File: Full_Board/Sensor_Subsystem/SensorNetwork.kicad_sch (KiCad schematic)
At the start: 34 parts, among them J12 OQ0432500000G, J13 OQ0432500000G, J14 OQ0432500000G, J15 OQ0432500000G, J16 OQ0432500000G, J17 OQ0432500000G, J18 OQ0432500000G, J19 OQ0432500000G, U13 UCLAMP3301H.TCT, U14 UCLAMP3301H.TCT, U15 SN74LV4051ATPWRQ1, U16 SN74LV4051ATPWRQ1

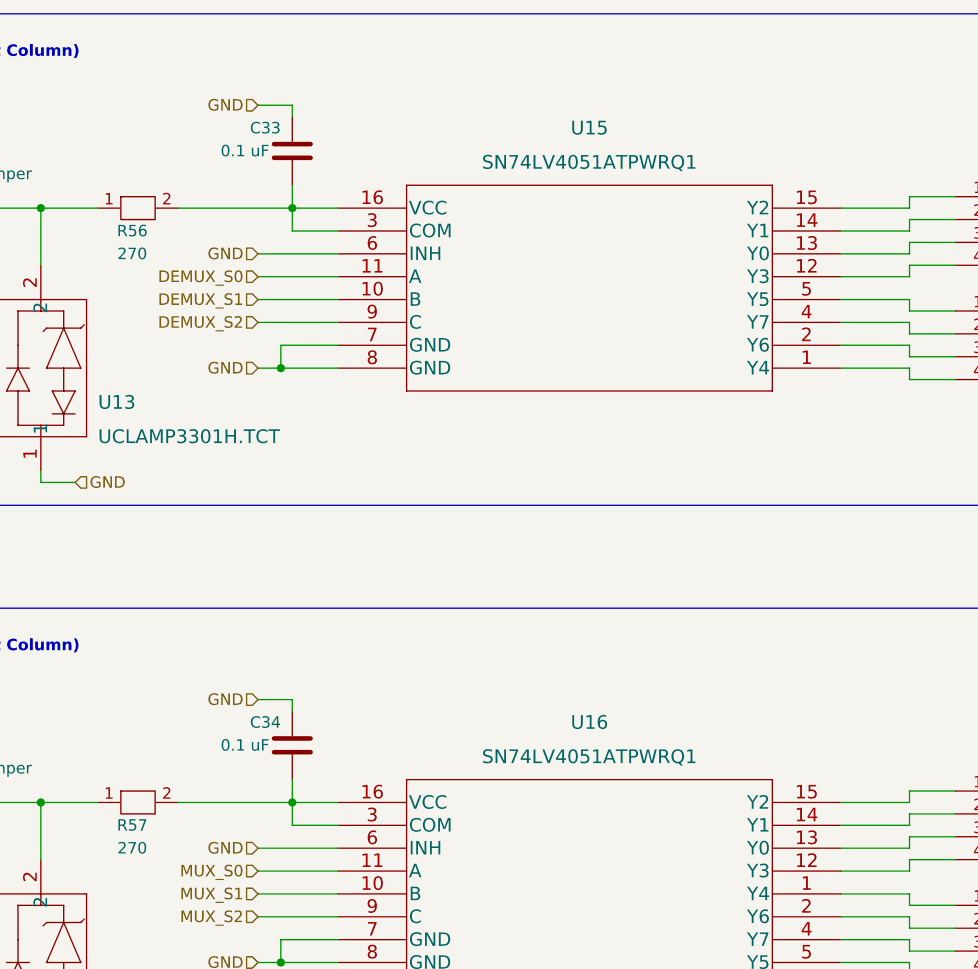
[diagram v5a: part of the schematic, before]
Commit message: Replaced electromagnet IC and fixed ERC errors with stepper driver
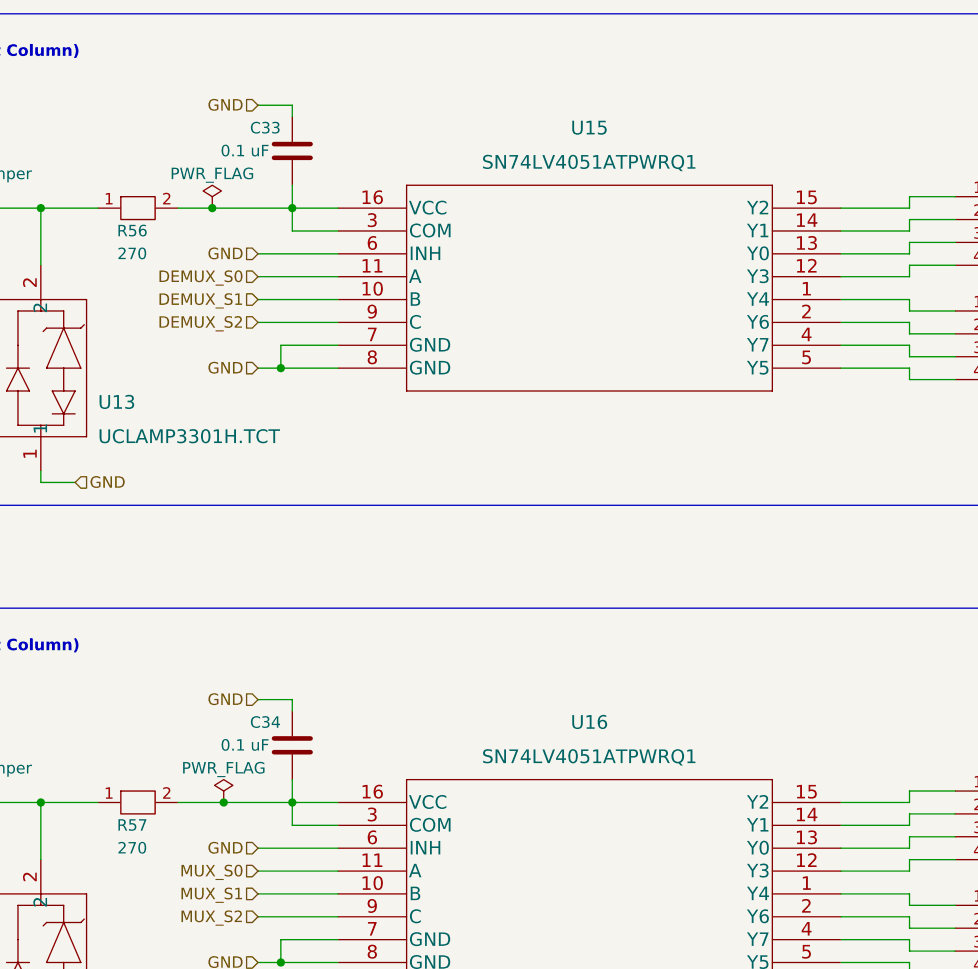
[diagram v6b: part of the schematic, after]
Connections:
- net at U15.1 (Y4): now also J13.1; no longer J13.4
- net at U15.2 (Y6): now also J13.2; no longer J13.3
- net at U15.4 (Y7): now also J13.3; no longer J13.2
- net at U15.5 (Y5): now also J13.4; no longer J13.1
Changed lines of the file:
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@@
   (junction (at 245.11 149.86) (diameter 0) (color 0 0 0 0)
   )
+  (junction (at 69.85 128.27) (diameter 0) (color 0 0 0 0)
+  )
   (junction (at 77.47 62.23) (diameter 0) (color 0 0 0 0)
   )
+  (junction (at 68.58 62.23) (diameter 0) (color 0 0 0 0)
+  )
   (wire (pts (xy 207.01 138.43) (xy 207.01 135.89))
     (stroke (width 0) (type default) (color 0 0 0 0))
@@
     (stroke (width 0) (type default) (color 0 0 0 0))
   )
-  (wire (pts (xy 64.77 128.27) (xy 77.47 128.27))
+  (wire (pts (xy 64.77 128.27) (xy 69.85 128.27))
     (stroke (width 0) (type default) (color 0 0 0 0))
   )
@@
     (stroke (width 0) (type default) (color 0 0 0 0))
   )
+  (wire (pts (xy 69.85 128.27) (xy 77.47 128.27))
+    (stroke (width 0) (type default) (color 0 0 0 0))
+  )
   (wire (pts (xy 265.43 72.39) (xy 265.43 73.66))
     (stroke (width 0) (type default) (color 0 0 0 0))
@@
     (stroke (width 0) (type default) (color 0 0 0 0))
   )
+  (wire (pts (xy 68.58 62.23) (xy 77.47 62.23))
+    (stroke (width 0) (type default) (color 0 0 0 0))
+  )
   (wire (pts (xy 77.47 59.69) (xy 77.47 62.23))
     (stroke (width 0) (type default) (color 0 0 0 0))
@@
     (stroke (width 0) (type default) (color 0 0 0 0))
   )
-  (wire (pts (xy 64.77 62.23) (xy 77.47 62.23))
+  (wire (pts (xy 64.77 62.23) (xy 68.58 62.23))
     (stroke (width 0) (type default) (color 0 0 0 0))
   )
@@
     (pin "1")
     (pin "2")
+  )
+  (symbol (lib_id "power:PWR_FLAG") (at 68.58 62.23 0) (unit 1)
+    (in_bom yes) (on_board yes)
+    (property "Reference" "#FLG0101" (id 0) (at 68.58 60.325 0)
+      (effects (font (size 1.27 1.27)) hide)
+    )
+    (property "Value" "PWR_FLAG" (id 1) (at 68.58 58.42 0))
+    (property "Footprint" "" (id 2) (at 68.58 62.23 0)
+      (effects (font (size 1.27 1.27)) hide)
+    )
+    (property "Datasheet" "~" (id 3) (at 68.58 62.23 0)
+      (effects (font (size 1.27 1.27)) hide)
+    )
+    (pin "1")
   )
   (symbol (lib_id "Device:C") (at 77.47 121.92 0) (mirror y) (unit 1)
@@
     (pin "2")
   )
-  (symbol (lib_name "SN74LV4051ATPWRQ1_1") (lib_id "SN74LV4051ATPWRQ1:SN74LV4051ATPWRQ1") (at 82.55 64.77 0) (unit 1)
+  (symbol (lib_id "SN74LV4051ATPWRQ1:SN74LV4051ATPWRQ1") (at 82.55 64.77 0) (unit 1)
     (in_bom yes) (on_board yes) (fields_autoplaced)
     (property "Reference" "U15" (id 0) (at 110.49 53.34 0)
@@
     (pin "9")
   )
+  (symbol (lib_id "power:PWR_FLAG") (at 69.85 128.27 0) (unit 1)
+    (in_bom yes) (on_board yes)
+    (property "Reference" "#FLG0102" (id 0) (at 69.85 126.365 0)
+      (effects (font (size 1.27 1.27)) hide)
+    )
+    (property "Value" "PWR_FLAG" (id 1) (at 69.85 124.46 0))
+    (property "Footprint" "" (id 2) (at 69.85 128.27 0)
+      (effects (font (size 1.27 1.27)) hide)
+    )
+    (property "Datasheet" "~" (id 3) (at 69.85 128.27 0)
+      (effects (font (size 1.27 1.27)) hide)
+    )
+    (pin "1")
+  )
   (symbol (lib_id "OQ04325500000G:OQ0432500000G") (at 248.92 135.89 90) (unit 1)

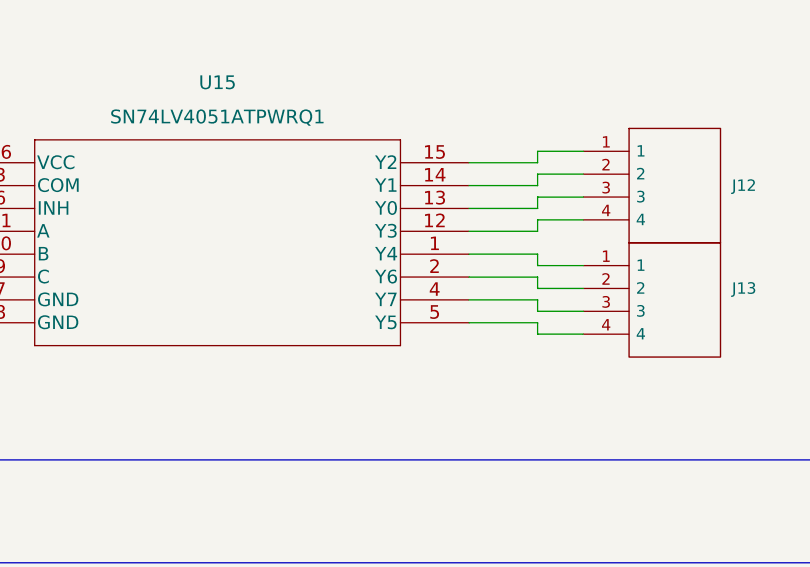
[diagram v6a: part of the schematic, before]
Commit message: Added traces for emag and increased the width of some power lines
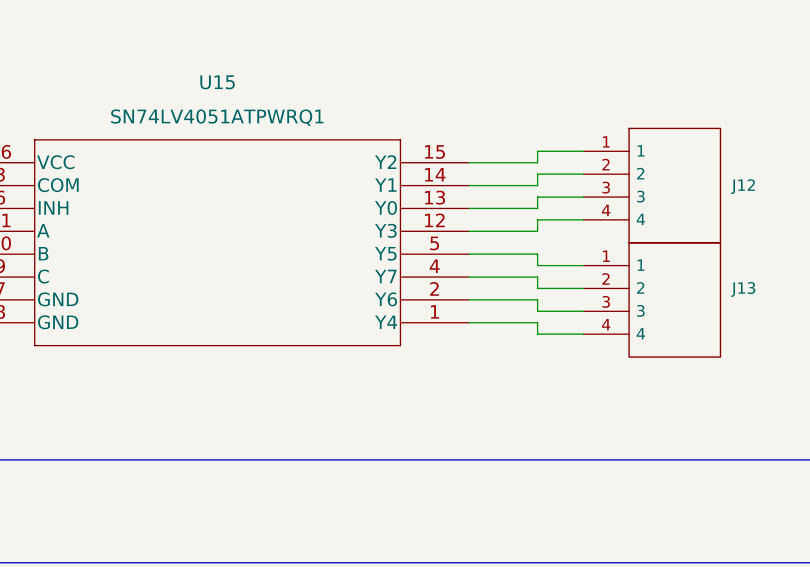
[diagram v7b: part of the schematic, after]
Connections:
- net at U15.1 (Y4): now also J13.4; no longer J13.1
- net at U15.2 (Y6): now also J13.3; no longer J13.2
- net at U15.4 (Y7): now also J13.2; no longer J13.3
- net at U15.5 (Y5): now also J13.1; no longer J13.4
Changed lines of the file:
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@@
     (pin "2")
   )
-  (symbol (lib_id "SN74LV4051ATPWRQ1:SN74LV4051ATPWRQ1") (at 82.55 64.77 0) (unit 1)
+  (symbol (lib_name "SN74LV4051ATPWRQ1_1") (lib_id "SN74LV4051ATPWRQ1:SN74LV4051ATPWRQ1") (at 82.55 64.77 0) (unit 1)
     (in_bom yes) (on_board yes) (fields_autoplaced)
     (property "Reference" "U15" (id 0) (at 110.49 53.34 0)

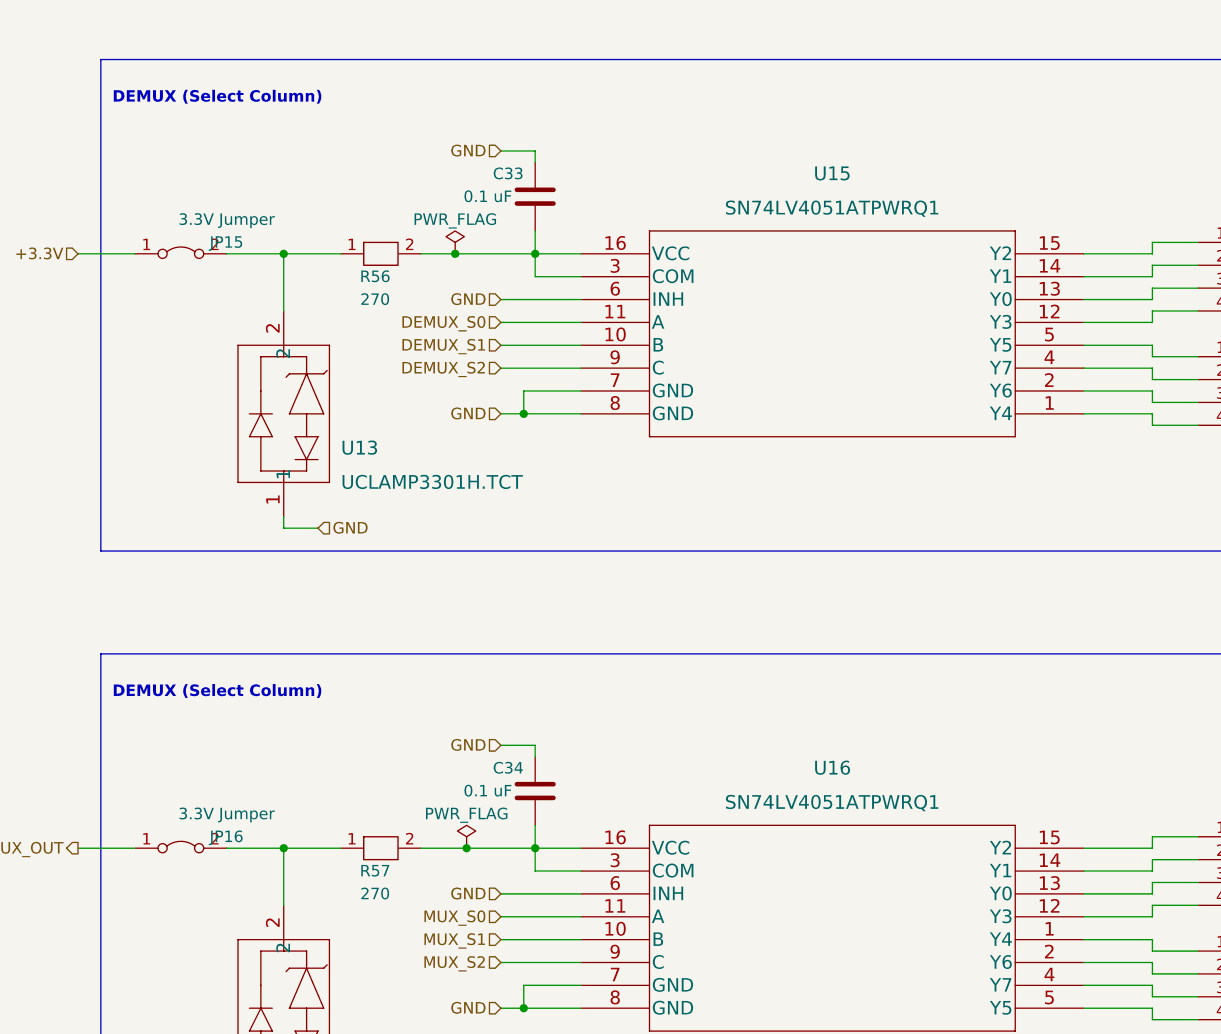
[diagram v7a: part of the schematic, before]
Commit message: Cleanup all schematics and project libs
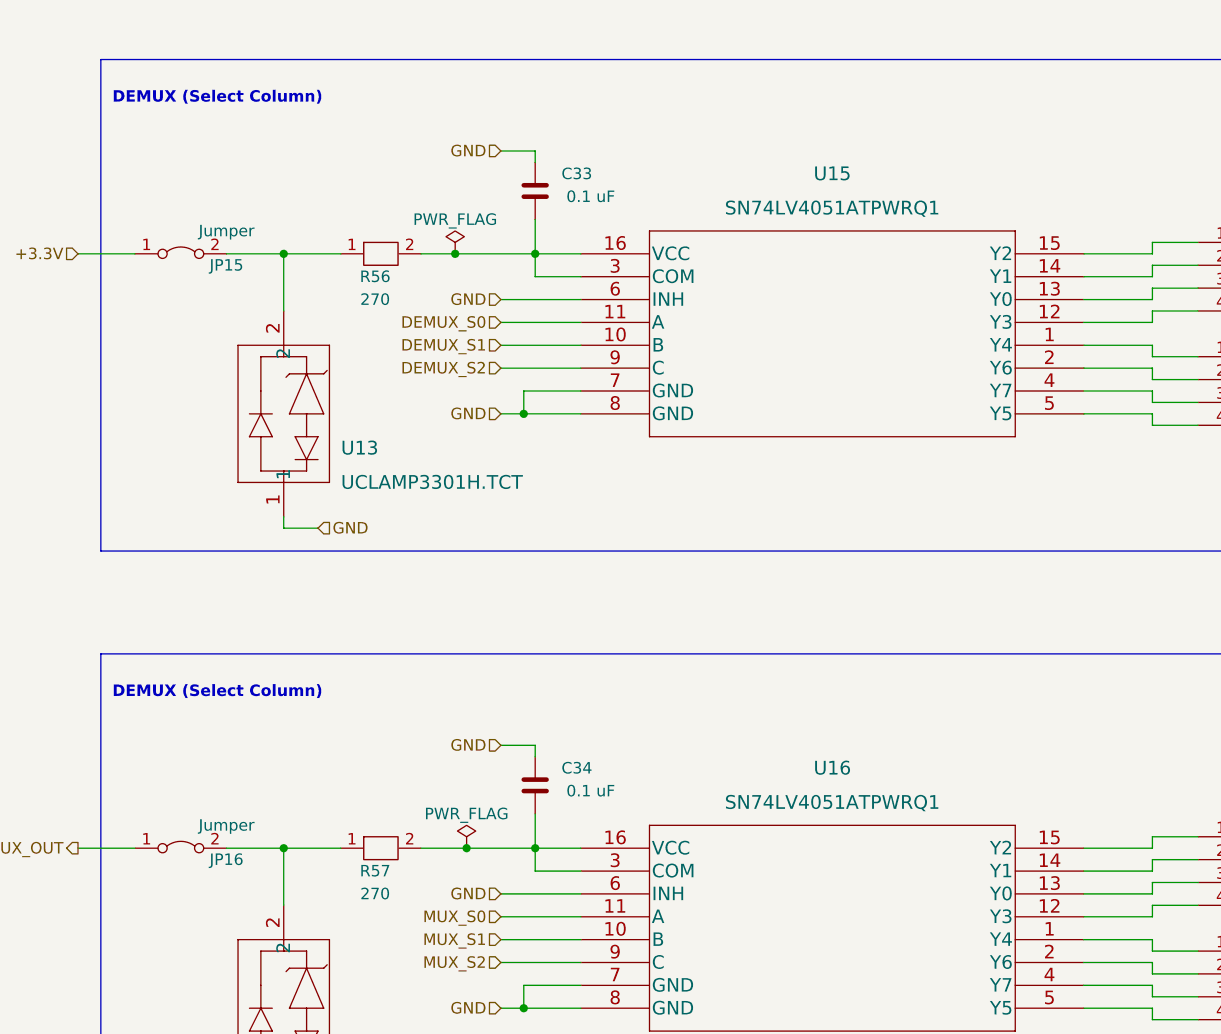
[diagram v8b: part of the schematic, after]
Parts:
- C33, C34: symbol Device:C -> CL10B104KB8NNC:CL10B104KB8NNNC; Digikey Link https://www.digikey.com/en/products/detail/samsung-electro-mechanics/CL10B104KB8NNNC/3886658 -> https://www.digikey.com/en/products/detail/samsung-electro-mechanics/CL10B104KB8NNNC/3886658?s=N4IgTCBcDaIMIBkCMAGAQqgLAaTQDgDki4QBdAXyA; Digikey Part Number 1276-1000-6-ND -> 1276-1000-1-ND; Manufacturer's Part Number (none) -> CL10B104KB8NNNC; Manufacturers Part Number CL10B104KB8NNNC -> (none); Mouser Link (none) -> https://www.mouser.com/ProductDetail/Samsung-Electro-Mechan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; Mouser Part Number (none) -> 187-CL10B104KB8NNNC
- J12, J13, J14, J15, J16, J17, J18, J19: Digikey link https://www.digikey.com/en/products/detail/amphenol-anytek/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 -> (none); Height 9.2 -> (none); Manufacturer_Name Amphenol -> (none); Manufacturer_Part_Number OQ0432500000G -> (none); Mouser Link (none) -> https://www.mouser.com/ProductDetail/Amphenol-Anytek/OQ0432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; Mouser Price/Stock https://www.mouser.co.uk/ProductDetail/Amphenol-Anytek/OQ04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 -> (none); Mouser link https://www.mouser.com/ProductDetail/Amphenol-Anytek/OQ0432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 -> (none)
- JP15, JP16: value 3.3V Jumper -> Jumper; symbol Jumper:Jumper_2_Bridged -> PH1-02-UA:PH1-02-UA; Digikey Link https://www.digikey.com/en/products/detail/adam-tech/PH1-02-UA/9830266 -> https://www.digikey.com/en/products/detail/adam-tech/PH1-02-UA/9830266?s=N4IgTCBcDa4AwFYDsBaACgCQIwrmFAqgIIoByAIiALoC%2BQA; Manufacturer's Part Number (none) -> PH1-02-UA; Manufacturers Part Number PH1-02-UA -> (none)
- R56, R57: Digikey Link (none) -> https://www.digikey.com/en/products/detail/rohm-semiconduct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; Digikey link https://www.digikey.com/en/products/detail/rohm-semiconduct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 -> (none); Mouser Link (none) -> https://www.mouser.com/ProductDetail/ROHM-Semiconductor/SDR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; Mouser link https://www.mouser.com/ProductDetail/ROHM-Semiconductor/SDR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 -> (none)
- R58, R59, R60, R61, R62, R63, R64, R65, R66, R67, R68, R69, R70, R71, R72, R73: Digikey Link (none) -> https://www.digikey.com/en/products/detail/stackpole-electr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; Digikey link https://www.digikey.com/en/products/detail/stackpole-electr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 -> (none)
- U13, U14: Manufacturer's Part Number (none) -> UCLAMP3301H.TCT; Manufacturers Part Number UCLAMP3301H.TCT -> (none); Mouser Link (none) -> https://www.mouser.com/ProductDetail/Semtech/UCLAMP3301H.TC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; Mouser Part Number (none) -> 947-UCLAMP3301H.TCT
- U15, U16: Digikey Link (none) -> https://www.digikey.com/en/products/detail/texas-instrument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; Digikey link https://www.digikey.com/en/products/detail/texas-instrument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 -> (none); Mouser Link (none) -> https://www.mouser.com/ProductDetail/Texas-Instruments/SN74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; Mouser link https://www.mouser.com/ProductDetail/Texas-Instruments/SN74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 -> (none)
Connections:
- net at U15.1 (Y4): now also J13.1; no longer J13.4
- net at U15.2 (Y6): now also J13.2; no longer J13.3
- net at U15.4 (Y7): now also J13.3; no longer J13.2
- net at U15.5 (Y5): now also J13.4; no longer J13.1
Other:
- moved on the sheet: C33, C34
